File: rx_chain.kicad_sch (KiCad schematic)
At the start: 5 parts, among them U21 ADL6331, U27 ADL8124, U30 ADL6332

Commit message: For Darrel
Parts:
- removed R121: 453k, Resistor_SMD:R_0402_1005Metric, symbol Device:R_Small
- removed R122: 33k, Resistor_SMD:R_0402_1005Metric, symbol Device:R_Small
- renumbered U27 to U19, U30 to U20
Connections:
- net GND: now also U21.1 (CA2), U21.23 (CA0), U21.24 (CA1)
- net EN_{AMP2}: now reaches U21.12 (EN)
- net RFOUT: now reaches U21.15 (RFOUT)
- net CIPO: now reaches U21.18 (SDO)
- net CIPO: now also U20.18 (SDO)
- net COPI: now reaches U21.19 (SDIO)
- net COPI: now also U20.19 (SDIO)
- net SCK: now reaches U21.20 (SCLK)
- net SCK: now also U20.20 (SCLK)
- net ~{CS_{AMP2}}: now reaches U21.21 (~{CS})
- net VTEMP: now reaches U19.4 (VTEMP)
- net EN_{AMP0}: now reaches U19.7 (EN)
- net EN_{AMP1}: now reaches U20.12 (EN)
- net ~{CS_{AMP1}}: now reaches U20.21 (~{CS})
- new net RFIN: U19.4 (VTEMP)
- no-connect marks 1 -> 6
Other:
- removed sheet Linear POL LMK DIG

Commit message: wip
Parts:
- added TP21: TPRXOUT, Connector_Coaxial:CoaxialSwitch_Hirose_MS-156C3_Horizontal, symbol Connector:CoaxialSwitch_Testpoint
- added TP22: TPRXIN, Connector_Coaxial:CoaxialSwitch_Hirose_MS-156C3_Horizontal, symbol Connector:CoaxialSwitch_Testpoint
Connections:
- net GND: now also U19.3 (GND), U19.6 (GND), U19.8 (GND), U19.9 (GND), U20.14 (GND), U20.17 (GND), U20.2 (GND), U20.25 (GND), U20.4 (GND), U20.5 (GND), U21.14 (GND), U21.16 (GND), U21.17 (GND), U21.2 (GND), U21.25 (GND), U21.5 (GND), TP21.G, TP22.G
- net RFOUT: now also TP22.C; no longer U21.15 (RFOUT)
- new net: TP21.A, TP22.A
- new net: TP21.C, U21.15 (RFOUT)

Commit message: wip
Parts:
- added C?: 100n, symbol Device:C_Feedthrough
- added R?: 1.54k, symbol Device:R_Small
- added R?: 33k, Resistor_SMD:R_0402_1005Metric, symbol Device:R_Small
- added R?: 453k, Resistor_SMD:R_0402_1005Metric, symbol Device:R_Small
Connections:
- net GND: now also C?.2, R?.2
- net VTEMP_AMP2: now reaches U21.7 (MUXOUT)
- net at U19.1 (RBIAS): now also R?.2
- net VTEMP_AMP1: now reaches U20.7 (MUXOUT)
- net VTEMP renamed VTEMP_LNA
- new net +3.3VA_LNA: C?.3, R?.1, U19.8 (GND)
- new net Linear POL LMK VCO/KELVIN: C?.1
- new net Linear POL LMK VCO/PGFB+: R?.1
- new net Linear POL LMK VCO/PGFB-: R?.2
- new net Linear POL LMK VCO/SET: R?.1
- no-connect marks 6 -> 5
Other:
- added sheet Linear POL LMK VCO (linear.kicad_sch)
- note added: "NOTE: Use LT3042 not 3045 for purposes of purchasing and assembly!"

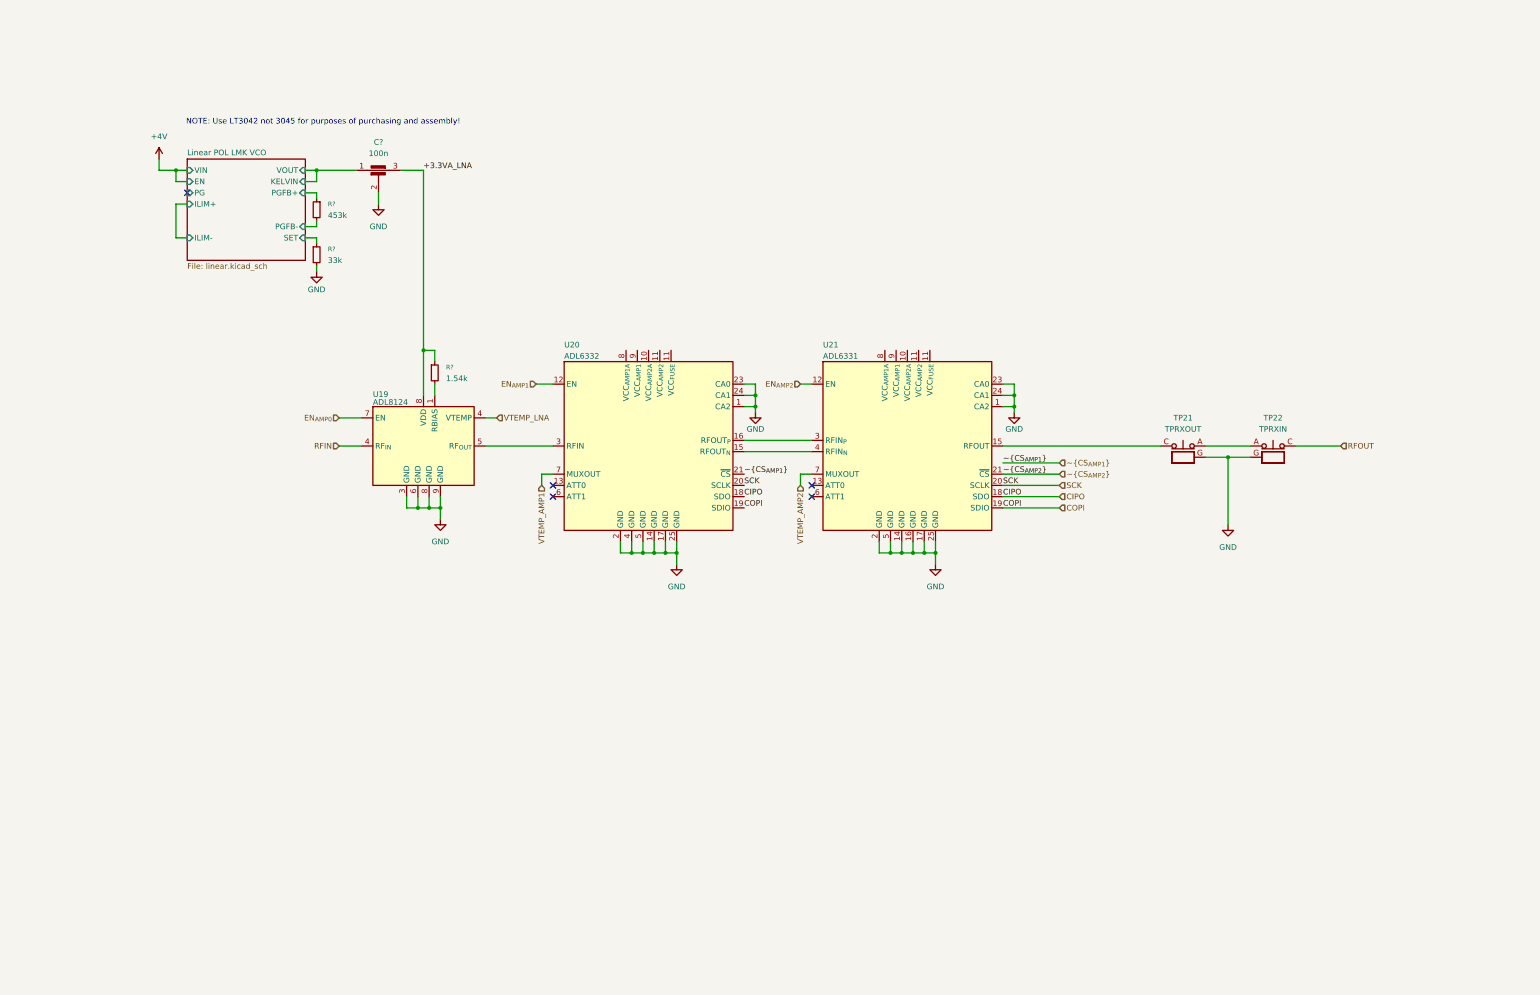
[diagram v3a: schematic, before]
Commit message: Rework RF Supplies
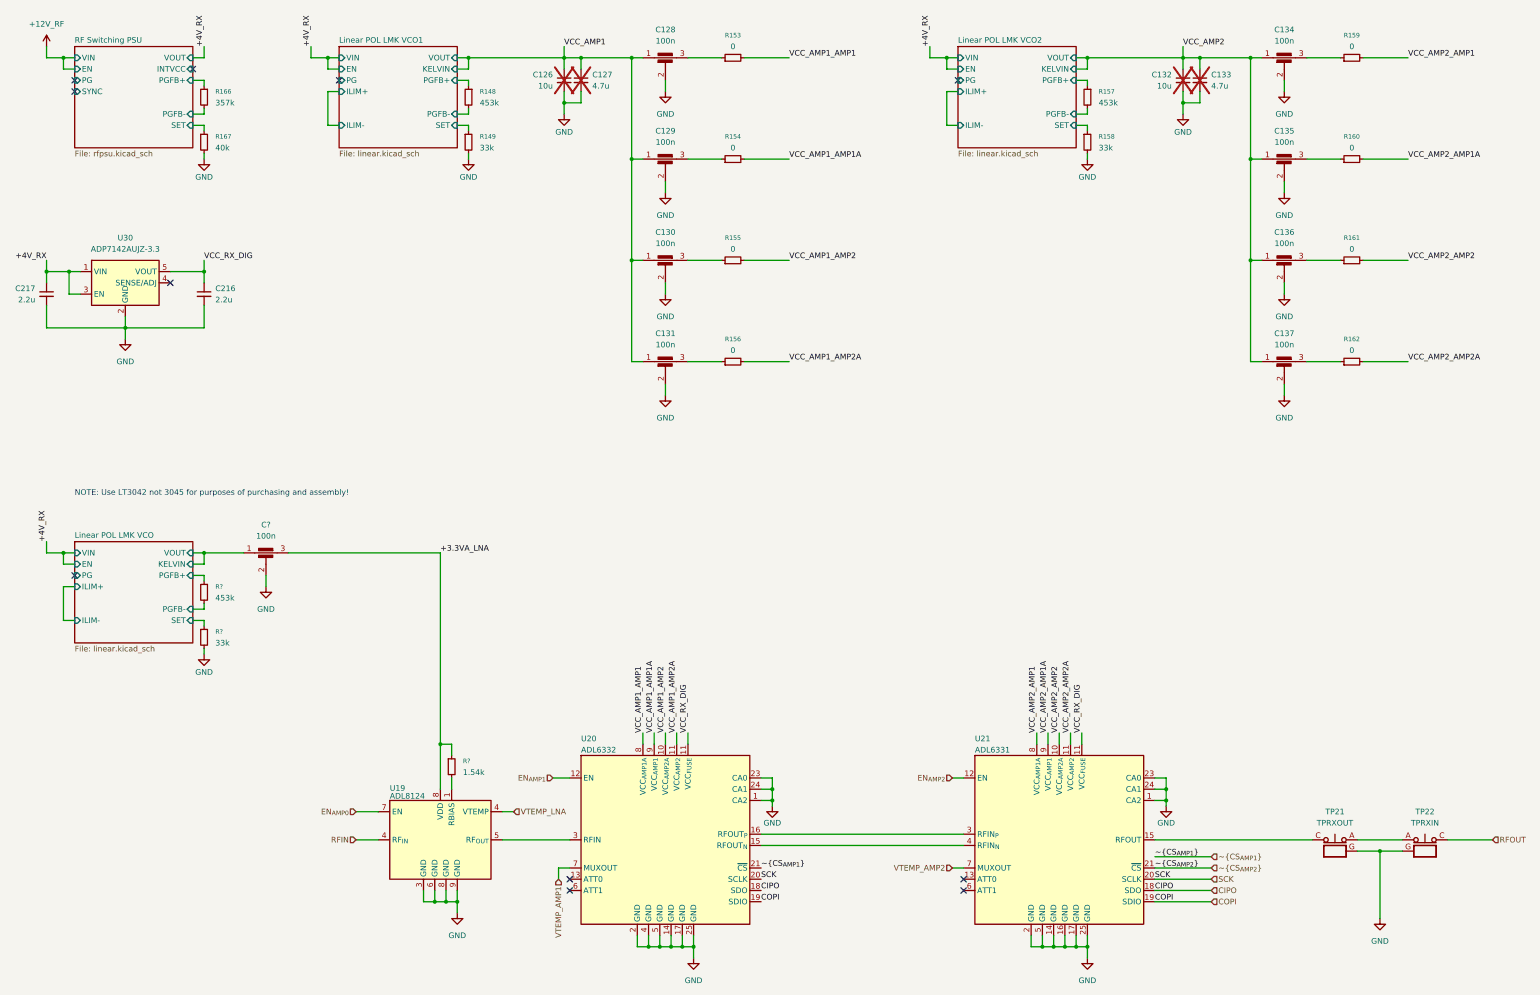
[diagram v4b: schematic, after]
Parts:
- added C126, C132: 10u, Capacitor_SMD:C_0603_1608Metric, symbol Device:C_Small
- added C127, C133: 4.7u, Capacitor_SMD:C_1206_3216Metric, symbol Device:C_Small
- added C128, C129, C130, C131, C134, C135, C136, C137: 100n, symbol Device:C_Feedthrough
- added C216, C217: 2.2u, symbol Device:C_Small
- added R148, R157: 453k, Resistor_SMD:R_0402_1005Metric, symbol Device:R_Small
- added R149, R158: 33k, Resistor_SMD:R_0402_1005Metric, symbol Device:R_Small
- added R153, R154, R155, R156, R159, R160, R161, R162: 0, Resistor_THT:R_Array_SIP4, symbol Device:R_Small
- added R166: 357k, Resistor_SMD:R_0402_1005Metric, symbol Device:R_Small
- added R167: 40k, Resistor_SMD:R_0402_1005Metric, symbol Device:R_Small
- added U30: ADP7142AUJZ-3.3, Package_TO_SOT_SMD:TSOT-23-5, symbol Regulator_Linear:ADP7142AUJZ-3.3
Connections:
- net GND: now also C126.2, C127.2, C128.2, C129.2, C130.2, C131.2, C132.2, C133.2, C134.2, C135.2, C136.2, C137.2, C216.2, C217.2, R149.2, R158.2, R167.2, U30.2 (GND)
- net VCC_AMP2_AMP2: now reaches U21.10 (VCC_{AMP2A})
- net VCC_AMP2_AMP2: now also R161.2
- net VCC_RX_DIG: now reaches U21.11 (VCC_{FUSE})
- net VCC_RX_DIG: now also U20.11 (VCC_{FUSE}), C216.1, U30.5 (VOUT)
- net VCC_AMP2_AMP1: now reaches U21.8 (VCC_{AMP1A})
- net VCC_AMP2_AMP1: now also R159.2
- net VCC_AMP2_AMP1A: now reaches U21.9 (VCC_{AMP1})
- net VCC_AMP2_AMP1A: now also R160.2
- net VCC_AMP1_AMP2: now reaches U20.10 (VCC_{AMP2A})
- net VCC_AMP1_AMP2: now also R155.2
- net VCC_AMP1_AMP1: now reaches U20.8 (VCC_{AMP1A})
- net VCC_AMP1_AMP1: now also R153.2
- net VCC_AMP1_AMP1A: now reaches U20.9 (VCC_{AMP1})
- net VCC_AMP1_AMP1A: now also R154.2
- new net: C137.3, R162.1
- new net: C135.3, R160.1
- new net: C136.3, R161.1
- new net: C129.3, R154.1
- new net: C130.3, R155.1
- new net: C131.3, R156.1
- new net: C128.3, R153.1
- new net: C134.3, R159.1
- new net +4V_RX: C217.1, U30.1 (VIN), U30.3 (EN)
- new net Linear POL LMK VCO1/PGFB+: R148.1
- new net Linear POL LMK VCO1/PGFB-: R148.2
- new net Linear POL LMK VCO1/SET: R149.1
- new net Linear POL LMK VCO2/PGFB+: R157.1
- new net Linear POL LMK VCO2/PGFB-: R157.2
- new net Linear POL LMK VCO2/SET: R158.1
- new net RF Switching PSU/PGFB+: R166.1
- new net RF Switching PSU/PGFB-: R166.2
- new net RF Switching PSU/SET: R167.1
- new net VCC_AMP1: C126.1, C127.1, C128.1, C129.1, C130.1, C131.1
- new net VCC_AMP1_AMP2A: R156.2, U20.11 (VCC_{FUSE})
- new net VCC_AMP2: C132.1, C133.1, C134.1, C135.1, C136.1, C137.1
- new net VCC_AMP2_AMP2A: R162.2, U21.11 (VCC_{FUSE})
- no-connect marks 5 -> 11
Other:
- added sheet Linear POL LMK VCO1 (linear.kicad_sch)
- added sheet Linear POL LMK VCO2 (linear.kicad_sch)
- added sheet RF Switching PSU (rfpsu.kicad_sch)
- moved on the sheet: C?, R?, TP21, TP22, U19, U20, U21

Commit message: Add Clock sources and monitor output
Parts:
- added U28: MEQ0-20ASM, Package_SO:MSOP-10_3x3mm_P0.5mm, symbol huskylib:MEQ0-20ASM
- added U29: MC16-0222SM, symbol huskylib:MC16-0222SM
- gave numbers to parts that had none: 4
- renumbered C217 to C129, C216 to C130, C126 to C132, C127 to C133, C128 to C134, C129 to C135, C130 to C136, C131 to C137, C132 to C138, C133 to C139, C134 to C140, C135 to C141, C136 to C142, C137 to C143, R166 to R136, R167 to R137, R148 to R139, R149 to R140, R153 to R141, R154 to R142, R155 to R143, R156 to R144, R157 to R145, R158 to R146, R159 to R147, R160 to R148, R161 to R149, R162 to R150, TP21 to TP10, TP22 to TP11, U30 to U24, U19 to U25, U20 to U26, U21 to U27
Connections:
- net GND: now also U28.10 (GND), U28.11 (GND), U28.12 (GND), U28.13 (GND), U28.2 (GND), U28.3 (GND), U28.4 (GND), U28.5 (GND), U28.6 (GND), U28.7 (GND), U28.8 (GND), U29.10 (GND), U29.12 (GND), U29.13 (GND), U29.14 (GND), U29.15 (GND), U29.16 (GND), U29.17 (GND), U29.18 (GND), U29.19 (GND), U29.2 (GND), U29.20 (GND), U29.21 (GND), U29.3 (GND), U29.4 (GND), U29.6 (GND), U29.7 (GND), U29.8 (GND)
- net at TP11.A: now also U29.11 (RFOUT); no longer TP10.A
- net at U27.15 (RFOUT): now also U28.1 (RFIN); no longer TP10.C
- new net: TP10.A, U29.5 (RFIN)
- new net: TP10.C, U28.9 (RFOUT)
- new net MONOUT: U29.1 (-16dB)
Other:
- moved on the sheet: C131, R134, R135, R138, TP10, TP11, U25, U26, U27

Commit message: It's finished (well the draft)
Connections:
- net VTEMP_LNA renamed VTEMP_AMP0
- no-connect marks 11 -> 9
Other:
- moved on the sheet: R136, R137

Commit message: Round 1 review comments
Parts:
- renumbered C129 to C170, C130 to C171, C131 to C172, C132 to C173, C133 to C174, C134 to C175, C135 to C176, C136 to C177, C137 to C178, C138 to C179, C139 to C180, C140 to C181, C141 to C182, C142 to C183, C143 to C184, R134 to R190, R135 to R191, R136 to R192, R137 to R193, R138 to R194, R139 to R195, R140 to R196, R141 to R197, R142 to R198, R143 to R199, R144 to R200, R145 to R201, R146 to R202, R147 to R203, R148 to R204, R149 to R205, R150 to R206, U24 to U26, U25 to U27, U26 to U28, U27 to U29, U28 to U30, U29 to U31
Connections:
- net Linear POL LMK VCO/PGFB+ is gone; now on net Linear POL LMK VCO/KELVIN: R190.1
- net Linear POL LMK VCO1/PGFB+ is gone; now on net VCC_AMP1: R195.1
- net Linear POL LMK VCO2/PGFB+ is gone; now on net VCC_AMP2: R201.1
- net VCC_RX_DIG: now also U26.4 (SENSE/ADJ)
- net Linear POL LMK VCO/PGFB- renamed Linear POL LMK VCO/PGFB
- net Linear POL LMK VCO1/PGFB- renamed Linear POL LMK VCO1/PGFB
- net Linear POL LMK VCO2/PGFB- renamed Linear POL LMK VCO2/PGFB
- no-connect marks 9 -> 8
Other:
- sheet Linear POL LMK VCO ports: added PGFB; removed PGFB+, PGFB-
- sheet Linear POL LMK VCO1 ports: added PGFB; removed PGFB+, PGFB-
- sheet Linear POL LMK VCO2 ports: added PGFB; removed PGFB+, PGFB-
- sheet RF Switching PSU ports: added OUTS; removed none

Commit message: Round 2 Review, power tree cleanup
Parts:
- removed C170, C171: 2.2u, symbol Device:C_Small
- removed U26: ADP7142AUJZ-3.3, Package_TO_SOT_SMD:TSOT-23-5, symbol Regulator_Linear:ADP7142AUJZ-3.3
- added C? (x2): 1u, symbol Device:C_Small
- added U?: TLV73333PDBV, Package_TO_SOT_SMD:SOT-23-5, symbol Regulator_Linear:TLV73333PDBV
- renumbered C172 to C174, C173 to C175, C174 to C176, C175 to C177, C176 to C178, C177 to C179, C178 to C180, C179 to C181, C180 to C182, C181 to C183, C182 to C184, C183 to C185, C184 to C186, R190 to R202, R191 to R203, R192 to R204, R193 to R205, R194 to R206, R195 to R207, R196 to R208, R197 to R209, R198 to R210, R199 to R211, R200 to R212, R201 to R213, R202 to R214, R203 to R215, R204 to R216, R205 to R217, R206 to R218
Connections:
- net +4V_RX: now also C?.1, U?.1 (IN), U?.3 (EN)
- net GND: now also C?.2, C?.2, U?.2 (GND)
- net VCC_RX_DIG: now also C?.1, U?.5 (OUT)
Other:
- sheet Linear POL LMK VCO1 renamed Linear POL AMP1
- sheet Linear POL LMK VCO2 renamed Linear POL LMK AMP2
